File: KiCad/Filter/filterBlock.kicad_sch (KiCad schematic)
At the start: 13 parts, among them U2 LTC1067-50

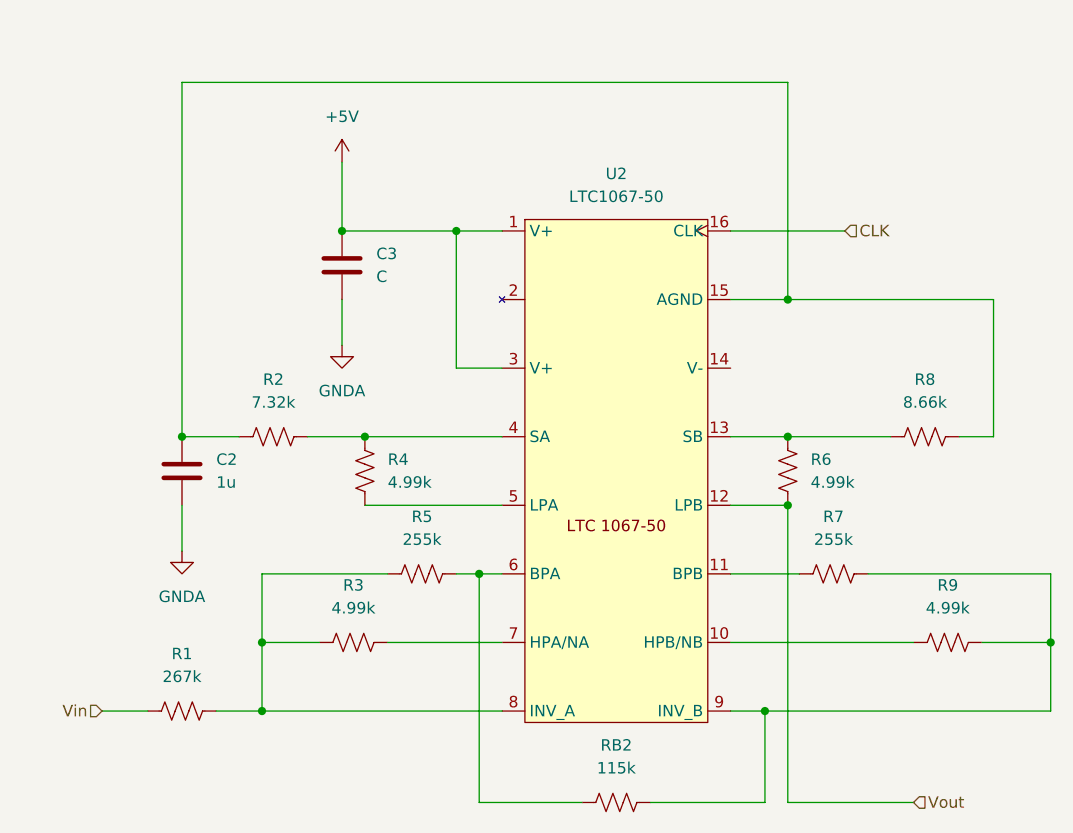
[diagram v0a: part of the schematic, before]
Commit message: Included MCP5211 in KiCad symbols
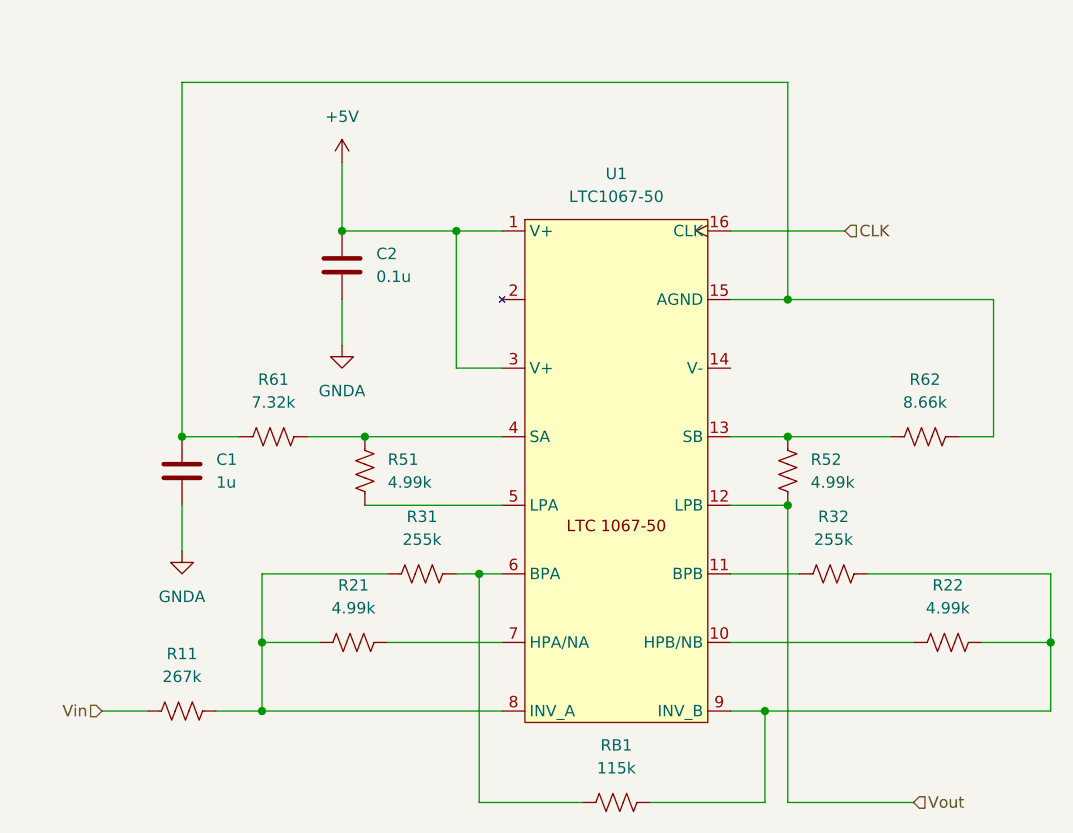
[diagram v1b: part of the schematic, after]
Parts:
- C2: renamed from C3; value C -> 0.1u
- renumbered C2 to C1, R1 to R11, R3 to R21, R9 to R22, R5 to R31, R7 to R32, R4 to R51, R6 to R52, R2 to R61, R8 to R62, RB2 to RB1, U2 to U1
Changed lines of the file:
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@@
 		(dnp no)
 		(fields_autoplaced yes)
-		(property "Reference" "R3"
+		(property "Reference" "R21"
 			(at 113.03 113.03 90)
 			(effects
@@
 			(project "Filter"
 				(path "/8ea2dc21-a8e6-4e4a-8986-17442369c6c0/62b2a83c-7ebf-4efa-a973-9882133fc683"
-					(reference "R3")
+					(reference "R21")
 					(unit 1)
 				)
@@
 		(dnp no)
 		(fields_autoplaced yes)
-		(property "Reference" "R5"
+		(property "Reference" "R31"
 			(at 120.65 105.41 90)
 			(effects
@@
 			(project "Filter"
 				(path "/8ea2dc21-a8e6-4e4a-8986-17442369c6c0/62b2a83c-7ebf-4efa-a973-9882133fc683"
-					(reference "R5")
+					(reference "R31")
 					(unit 1)
 				)
@@
 		(dnp no)
 		(fields_autoplaced yes)
-		(property "Reference" "R4"
+		(property "Reference" "R51"
 			(at 116.84 99.0599 0)
 			(effects
@@
 			(project "Filter"
 				(path "/8ea2dc21-a8e6-4e4a-8986-17442369c6c0/62b2a83c-7ebf-4efa-a973-9882133fc683"
-					(reference "R4")
+					(reference "R51")
 					(unit 1)
 				)
@@
 		(dnp no)
 		(fields_autoplaced yes)
-		(property "Reference" "R1"
+		(property "Reference" "R11"
 			(at 93.98 120.65 90)
 			(effects
@@
 			(project "Filter"
 				(path "/8ea2dc21-a8e6-4e4a-8986-17442369c6c0/62b2a83c-7ebf-4efa-a973-9882133fc683"
-					(reference "R1")
+					(reference "R11")
 					(unit 1)
 				)
@@
 		(dnp no)
 		(fields_autoplaced yes)
-		(property "Reference" "R6"
+		(property "Reference" "R52"
 			(at 163.83 99.0599 0)
 			(effects
@@
 			(project "Filter"
 				(path "/8ea2dc21-a8e6-4e4a-8986-17442369c6c0/62b2a83c-7ebf-4efa-a973-9882133fc683"
-					(reference "R6")
+					(reference "R52")
 					(unit 1)
 				)
@@
 		(dnp no)
 		(fields_autoplaced yes)
-		(property "Reference" "RB2"
+		(property "Reference" "RB1"
 			(at 142.24 130.81 90)
 			(effects
@@
 			(project "Filter"
 				(path "/8ea2dc21-a8e6-4e4a-8986-17442369c6c0/62b2a83c-7ebf-4efa-a973-9882133fc683"
-					(reference "RB2")
+					(reference "RB1")
 					(unit 1)
 				)
@@
 		(dnp no)
 		(fields_autoplaced yes)
-		(property "Reference" "R2"
+		(property "Reference" "R61"
 			(at 104.14 90.17 90)
 			(effects
@@
 			(project "Filter"
 				(path "/8ea2dc21-a8e6-4e4a-8986-17442369c6c0/62b2a83c-7ebf-4efa-a973-9882133fc683"
-					(reference "R2")
+					(reference "R61")
 					(unit 1)
 				)
@@
 		(dnp no)
 		(fields_autoplaced yes)
-		(property "Reference" "R8"
+		(property "Reference" "R62"
 			(at 176.53 90.17 90)
 			(effects
@@
 			(project "Filter"
 				(path "/8ea2dc21-a8e6-4e4a-8986-17442369c6c0/62b2a83c-7ebf-4efa-a973-9882133fc683"
-					(reference "R8")
+					(reference "R62")
 					(unit 1)
 				)
@@
 		(dnp no)
 		(fields_autoplaced yes)
-		(property "Reference" "R9"
+		(property "Reference" "R22"
 			(at 179.07 113.03 90)
 			(effects
@@
 			(project "Filter"
 				(path "/8ea2dc21-a8e6-4e4a-8986-17442369c6c0/62b2a83c-7ebf-4efa-a973-9882133fc683"
-					(reference "R9")
+					(reference "R22")
 					(unit 1)
 				)
@@
 		(dnp no)
 		(fields_autoplaced yes)
-		(property "Reference" "R7"
+		(property "Reference" "R32"
 			(at 166.37 105.41 90)
 			(effects
@@
 			(project "Filter"
 				(path "/8ea2dc21-a8e6-4e4a-8986-17442369c6c0/62b2a83c-7ebf-4efa-a973-9882133fc683"
-					(reference "R7")
+					(reference "R32")
 					(unit 1)
 				)
@@
 		(dnp no)
 		(fields_autoplaced yes)
-		(property "Reference" "U2"
+		(property "Reference" "U1"
 			(at 142.24 67.31 0)
 			(effects
@@
 			(project "Filter"
 				(path "/8ea2dc21-a8e6-4e4a-8986-17442369c6c0/62b2a83c-7ebf-4efa-a973-9882133fc683"
-					(reference "U2")
+					(reference "U1")
 					(unit 1)
 				)
@@
 		(dnp no)
 		(fields_autoplaced yes)
-		(property "Reference" "C3"
+		(property "Reference" "C2"
 			(at 115.57 76.1999 0)
 			(effects
@@
 			)
 		)
-		(property "Value" "C"
+		(property "Value" "0.1u"
 			(at 115.57 78.7399 0)
 			(effects
@@
 			(project ""
 				(path "/8ea2dc21-a8e6-4e4a-8986-17442369c6c0/62b2a83c-7ebf-4efa-a973-9882133fc683"
-					(reference "C3")
+					(reference "C2")
 					(unit 1)
 				)
@@
 		(dnp no)
 		(fields_autoplaced yes)
-		(property "Reference" "C2"
+		(property "Reference" "C1"
 			(at 97.79 99.0599 0)
 			(effects
@@
 			(project "Filter"
 				(path "/8ea2dc21-a8e6-4e4a-8986-17442369c6c0/62b2a83c-7ebf-4efa-a973-9882133fc683"
-					(reference "C2")
-					(unit 1)
-				)
+					(reference "C1")
+					(unit 1)
+				)

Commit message: filterBlock updates. Filter proof of concept has been breadboarded and tested with with similiar standard value resistors. Works but the output is ~5Hz faster than input signal.
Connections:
- net GNDA: now also U1.14 (V-)
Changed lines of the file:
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@@
+	(wire
+		(pts
+			(xy 154.94 88.9) (xy 165.1 88.9)
+		)
+		(stroke
+			(width 0)
+			(type default)
+		)
+	)
 	(wire
 		(pts
@@
 					(unit 1)
 				)
+			)
+		)
+	)
+	(symbol
+		(lib_id "power:GNDA")
+		(at 165.1 88.9 0)
+		(unit 1)
+		(exclude_from_sim no)
+		(in_bom yes)
+		(on_board yes)
+		(dnp no)
+		(fields_autoplaced yes)
+		(property "Reference" "#PWR01"
+			(at 165.1 95.25 0)
+			(effects
+				(font
+					(size 1.27 1.27)
+				)
+				(hide yes)
+			)
+		)
+		(property "Value" "GNDA"
+			(at 165.1 93.98 0)
+			(effects
+				(font
+					(size 1.27 1.27)
+				)
+			)
+		)
+		(property "Footprint" ""
+			(at 165.1 88.9 0)
+			(effects
+				(font
+					(size 1.27 1.27)
+				)
+				(hide yes)
+			)
+		)
+		(property "Datasheet" ""
+			(at 165.1 88.9 0)
+			(effects
+				(font
+					(size 1.27 1.27)
+				)
+				(hide yes)
+			)
+		)
+		(property "Description" "Power symbol creates a global label with name \"GNDA\" , analog ground"
+			(at 165.1 88.9 0)
+			(effects
+				(font
+					(size 1.27 1.27)
+				)
+				(hide yes)
+			)
+		)
+		(pin "1"
+		)
+		(instances
+			(project "Filter"
+				(path "/8ea2dc21-a8e6-4e4a-8986-17442369c6c0/62b2a83c-7ebf-4efa-a973-9882133fc683"
+					(reference "#PWR01")
+					(unit 1)
+				)

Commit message: Added optional Correction Caps.
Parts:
- added C4, C5, C6, C7, C8, C9: C, symbol Device:C
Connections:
- net Vout: now also C7.1, C8.1, C9.1
- net INV_A: now reaches R11.2, R21.1, R31.1, U1.8 (INV_A)
- net INV_A: now also C4.2, C5.2, C6.2
- net LPA: now reaches R51.1, U1.5 (LPA)
- net LPA: now also C4.1, C5.1, C6.1
- net INV_B: now reaches R22.2, R32.2, RB1.2, U1.9 (INV_B)
- net INV_B: now also C7.2, C8.2, C9.2
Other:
- note added: "Optional correction capacitors(C6-C9) are available if filter needs tuning. Do not Populate."

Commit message: Added input jacks and bypass switch. Finished pwr supply except for 9v connection.
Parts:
- C4, C5, C6, C7, C8, C9: now not fitted
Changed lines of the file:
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@@
 		(in_bom yes)
 		(on_board yes)
-		(dnp no)
+		(dnp yes)
 		(fields_autoplaced yes)
 		(property "Reference" "C8"
@@
 		(in_bom yes)
 		(on_board yes)
-		(dnp no)
+		(dnp yes)
 		(fields_autoplaced yes)
 		(property "Reference" "C5"
@@
 		(in_bom yes)
 		(on_board yes)
-		(dnp no)
+		(dnp yes)
 		(fields_autoplaced yes)
 		(property "Reference" "C7"
@@
 		(in_bom yes)
 		(on_board yes)
-		(dnp no)
+		(dnp yes)
 		(fields_autoplaced yes)
 		(property "Reference" "C9"
@@
 		(in_bom yes)
 		(on_board yes)
-		(dnp no)
+		(dnp yes)
 		(fields_autoplaced yes)
 		(property "Reference" "C6"
@@
 		(in_bom yes)
 		(on_board yes)
-		(dnp no)
+		(dnp yes)
 		(fields_autoplaced yes)
 		(property "Reference" "C4"
